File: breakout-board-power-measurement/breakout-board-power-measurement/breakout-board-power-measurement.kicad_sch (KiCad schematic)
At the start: 62 parts, among them J1 Screw_Terminal_01x04, J2 Conn_01x09, J3 Conn_01x07, J4 Conn_01x02, U1 MCP3911A0-E-SS, U2 Si8641BA-B-IU, U3 LM317_TO-252, Y1 10M

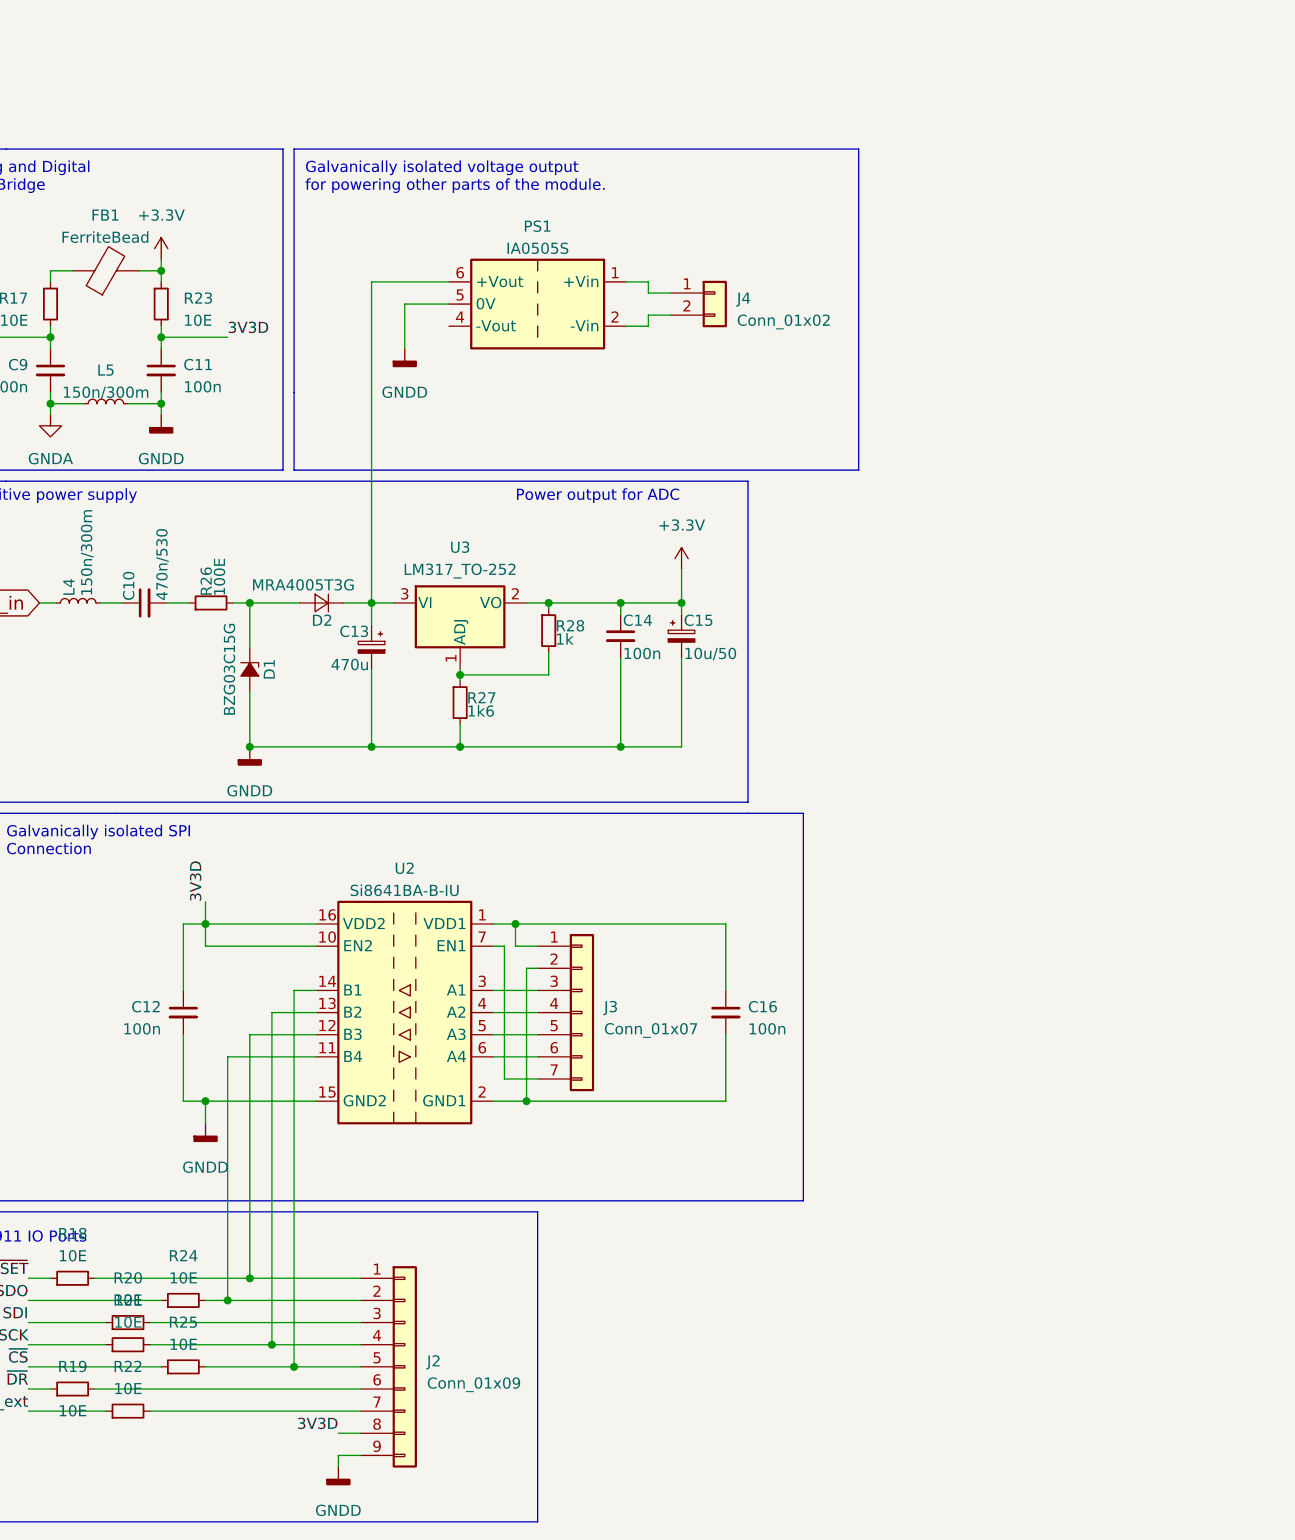
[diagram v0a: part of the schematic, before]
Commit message: Changed vias to test points
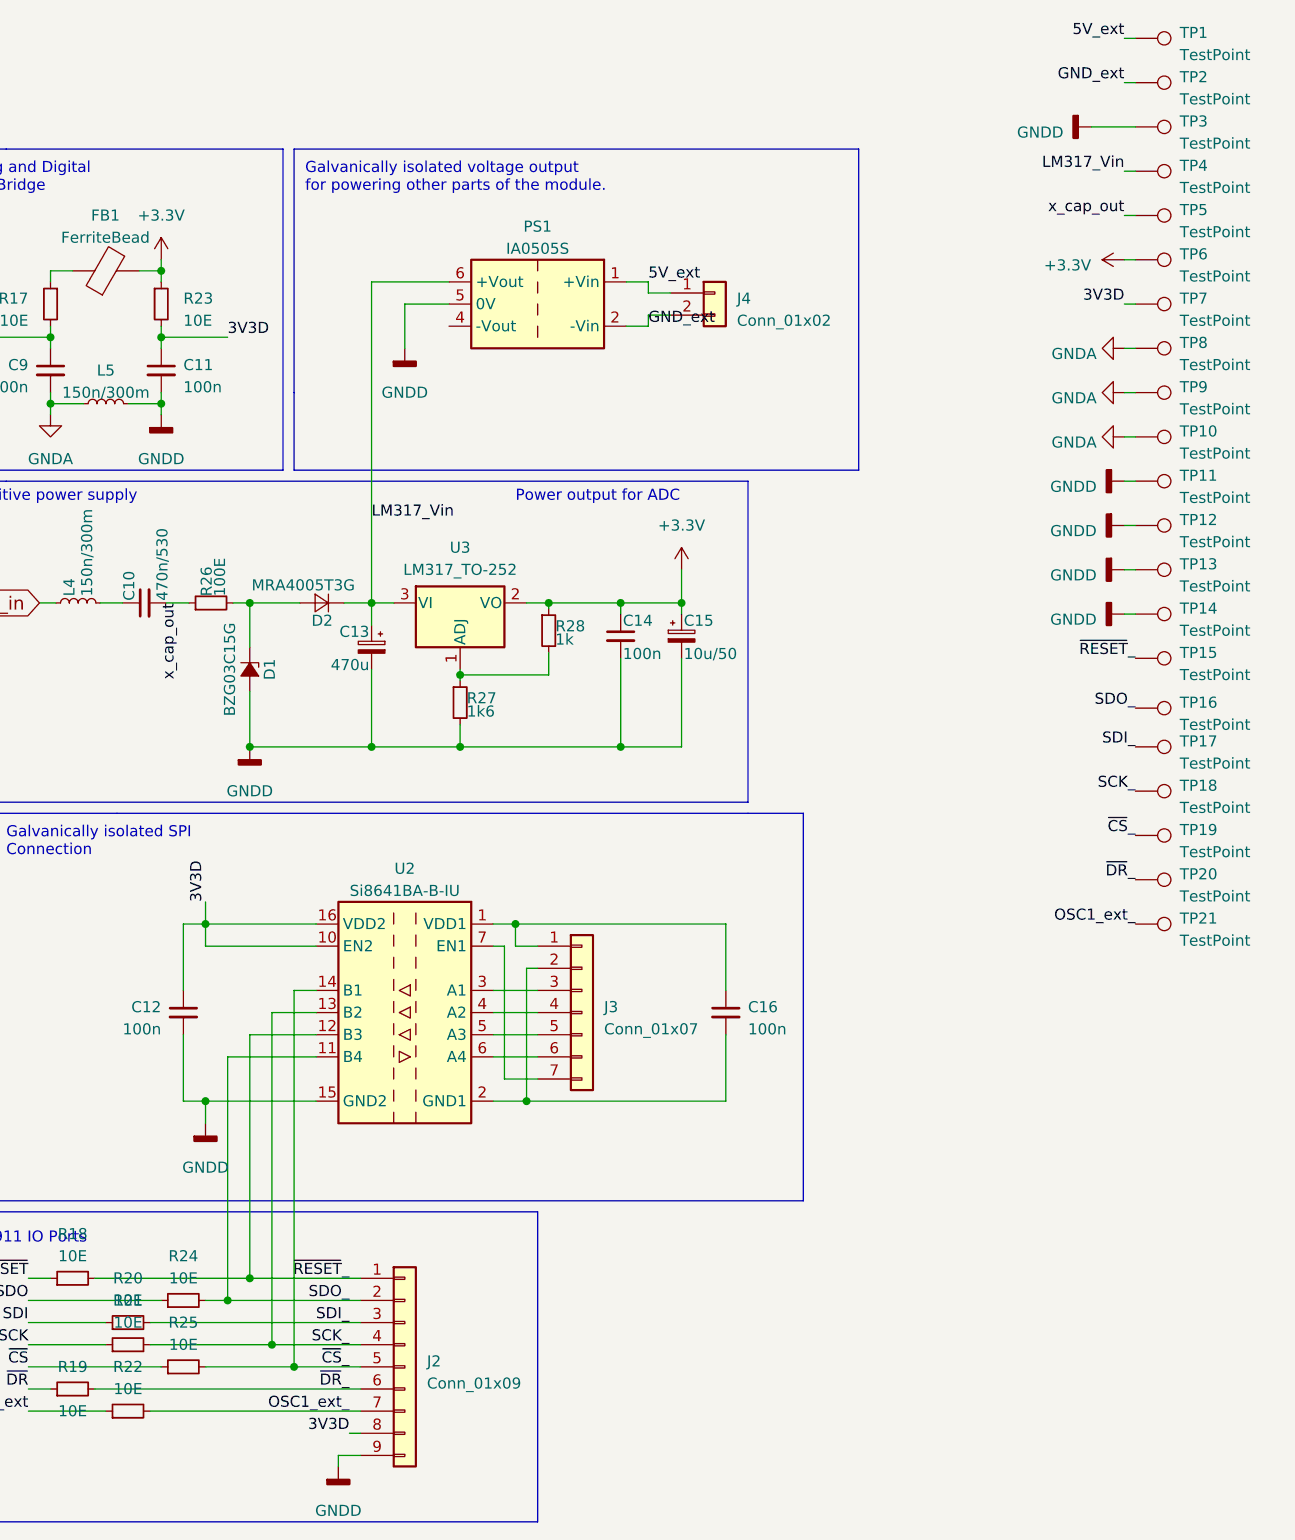
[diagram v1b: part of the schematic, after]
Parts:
- added TP1, TP10, TP11, TP12, TP13, TP14, TP15, TP16, TP17, TP18, TP19, TP2, TP20, TP21, TP3, TP4, TP5, TP6, TP7, TP8, TP9: TestPoint, TestPoint:TestPoint_THTPad_D1.0mm_Drill0.5mm, symbol Connector:TestPoint
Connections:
- net +3.3V: now also TP6.1
- net 3V3D: now also TP7.1
- net GNDA: now also TP10.1, TP8.1, TP9.1
- net GNDD: now also TP11.1, TP12.1, TP13.1, TP14.1, TP3.1
- net x_cap_out: now reaches C10.2, R26.1
- net x_cap_out: now also TP5.1
- net ~{RESET}_: now reaches J2.1 (Pin_1), R18.2, U2.12 (B3)
- net ~{RESET}_: now also TP15.1
- net SDO_: now reaches J2.2 (Pin_2), R24.2, U2.11 (B4)
- net SDO_: now also TP16.1
- net SDI_: now reaches J2.3 (Pin_3), R20.2
- net SDI_: now also TP17.1
- net SCK_: now reaches J2.4 (Pin_4), R21.2, U2.13 (B2)
- net SCK_: now also TP18.1
- net ~{CS}_: now reaches J2.5 (Pin_5), R25.2, U2.14 (B1)
- net ~{CS}_: now also TP19.1
- net ~{DR}_: now reaches J2.6 (Pin_6), R19.2
- net ~{DR}_: now also TP20.1
- net OSC1_ext_: now reaches J2.7 (Pin_7), R22.2
- net OSC1_ext_: now also TP21.1
- net 5V_ext: now reaches J4.1 (Pin_1), PS1.1 (+Vin)
- net 5V_ext: now also TP1.1
- net GND_ext: now reaches J4.2 (Pin_2), PS1.2 (-Vin)
- net GND_ext: now also TP2.1
- net LM317_Vin: now reaches C13.1, D2.1 (K), PS1.6 (+Vout), U3.3 (VI)
- net LM317_Vin: now also TP4.1

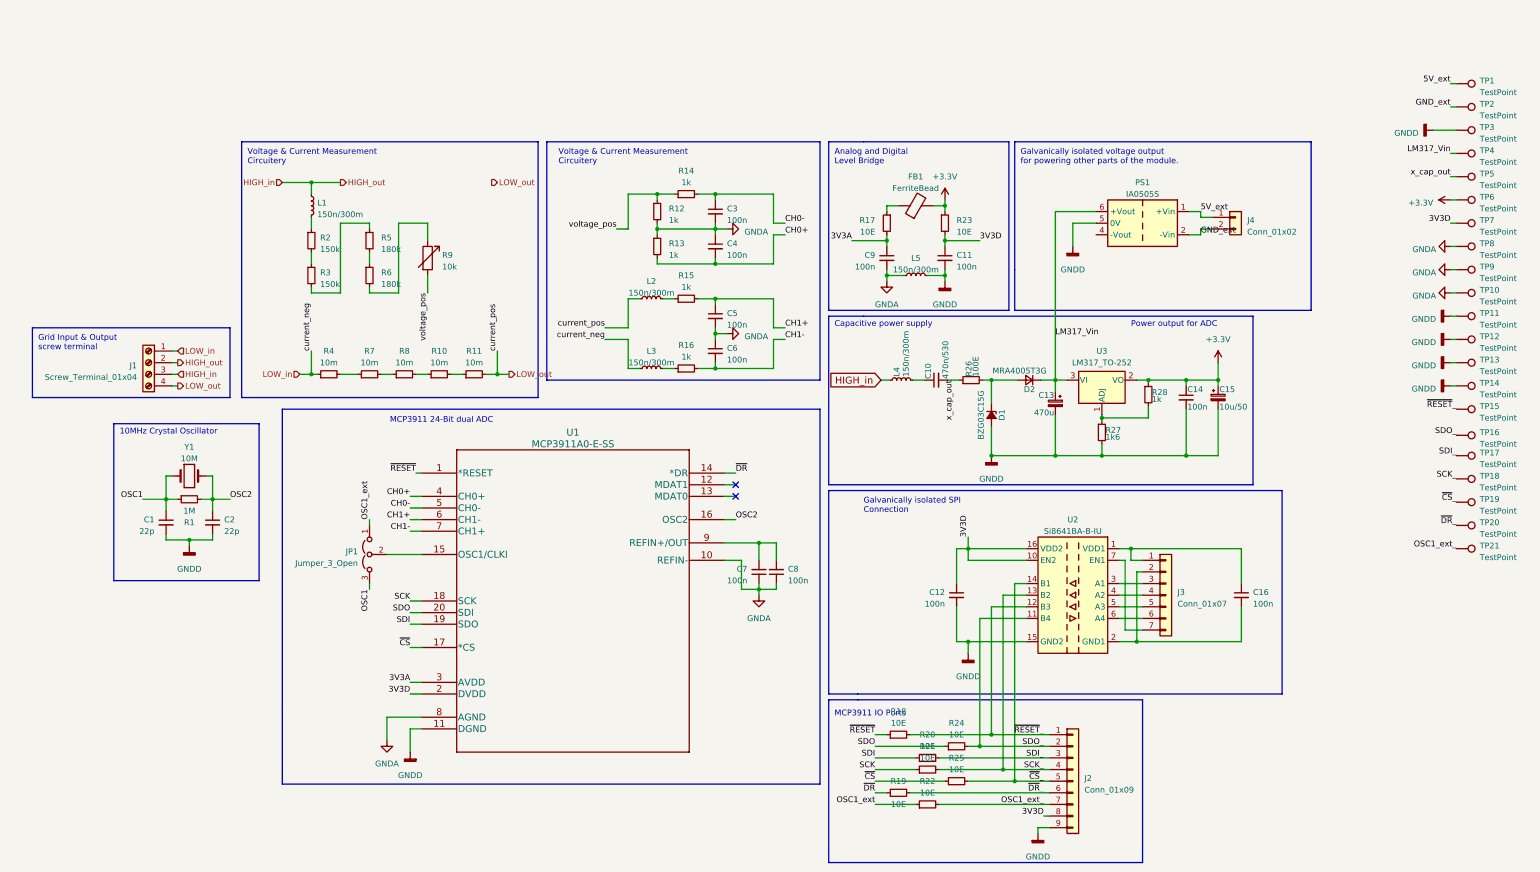
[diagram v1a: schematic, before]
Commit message: Fixed Power Measurement PCB, important changes.
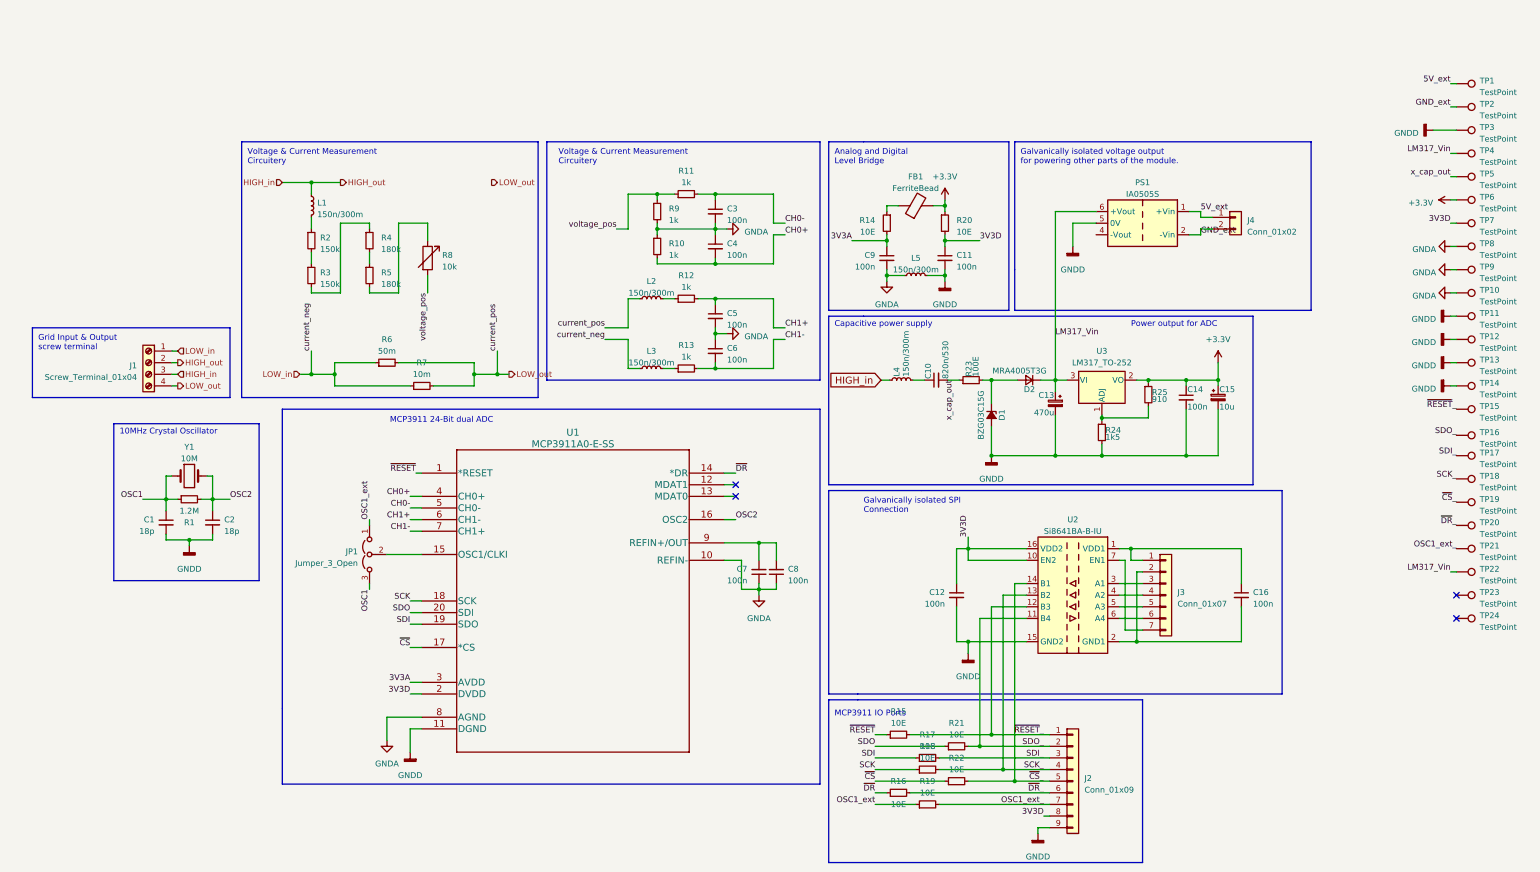
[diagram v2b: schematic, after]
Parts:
- removed R11, R4, R8: 10m, Resistor_SMD:R_1210_3225Metric, symbol Device:R_Small
- added TP22: TestPoint, Via:Via_THTPad_D1.5mm_Drill0.8mm, symbol Connector:TestPoint
- added TP23, TP24: TestPoint, Screwhole:Screwhole_THTPad_D3.0mm_Drill2.0mm, symbol Connector:TestPoint
- C1, C2: value 22p -> 18p
- C10: value 470n/530 -> 820n/530
- C13: footprint Capacitor_Tantalum_SMD:CP_EIA-7343-31_Kemet-D_Pad2.25x2.55mm_HandSolder -> Capacitor_THT:CP_Radial_D10.0mm_P5.00mm
- C15: value 10u/50 -> 10u; footprint Capacitor_Tantalum_SMD:CP_EIA-7343-31_Kemet-D_Pad2.25x2.55mm_HandSolder -> Capacitor_SMD:C_1206_3216Metric_Pad1.33x1.80mm_HandSolder
- D2: footprint Diode_SMD:D_SMA-SMB_Universal_Handsoldering -> Diode_SMD:D_MicroMELF_Handsoldering
- FB1: footprint Diode_SMD:D_SMA-SMB_Universal_Handsoldering -> Inductor_SMD:L_1210_3225Metric_Pad1.42x2.65mm_HandSolder
- R1: value 1M -> 1.2M
- R14: renamed from R17; footprint Resistor_SMD:R_1206_3216Metric_Pad1.30x1.75mm_HandSolder -> Resistor_SMD:R_0805_2012Metric_Pad1.20x1.40mm_HandSolder
- R15: renamed from R18; footprint Resistor_SMD:R_1206_3216Metric_Pad1.30x1.75mm_HandSolder -> Resistor_SMD:R_0805_2012Metric_Pad1.20x1.40mm_HandSolder
- R16: renamed from R19; footprint Resistor_SMD:R_1206_3216Metric_Pad1.30x1.75mm_HandSolder -> Resistor_SMD:R_0805_2012Metric_Pad1.20x1.40mm_HandSolder
- R17: renamed from R20; footprint Resistor_SMD:R_1206_3216Metric_Pad1.30x1.75mm_HandSolder -> Resistor_SMD:R_0805_2012Metric_Pad1.20x1.40mm_HandSolder
- R18: renamed from R21; footprint Resistor_SMD:R_1206_3216Metric_Pad1.30x1.75mm_HandSolder -> Resistor_SMD:R_0805_2012Metric_Pad1.20x1.40mm_HandSolder
- R19: renamed from R22; footprint Resistor_SMD:R_1206_3216Metric_Pad1.30x1.75mm_HandSolder -> Resistor_SMD:R_0805_2012Metric_Pad1.20x1.40mm_HandSolder
- R20: renamed from R23; footprint Resistor_SMD:R_1206_3216Metric_Pad1.30x1.75mm_HandSolder -> Resistor_SMD:R_0805_2012Metric_Pad1.20x1.40mm_HandSolder
- R21: renamed from R24; footprint Resistor_SMD:R_1206_3216Metric_Pad1.30x1.75mm_HandSolder -> Resistor_SMD:R_0805_2012Metric_Pad1.20x1.40mm_HandSolder
- R22: renamed from R25; footprint Resistor_SMD:R_1206_3216Metric_Pad1.30x1.75mm_HandSolder -> Resistor_SMD:R_0805_2012Metric_Pad1.20x1.40mm_HandSolder
- R24: renamed from R27; value 1k6 -> 1k5
- R25: renamed from R28; value 1k -> 910
- R6: renamed from R7; value 10m -> 50m; footprint Resistor_SMD:R_1210_3225Metric -> Resistor_SMD:R_2512_6332Metric
- R7: renamed from R10; footprint Resistor_SMD:R_1210_3225Metric -> Resistor_SMD:R_2512_6332Metric
- TP1, TP10, TP11, TP12, TP13, TP14, TP15, TP16, TP17, TP18, TP19, TP2, TP20, TP21, TP3, TP4, TP5, TP6, TP7, TP8, TP9: footprint TestPoint:TestPoint_THTPad_D1.0mm_Drill0.5mm -> Via:Via_THTPad_D1.5mm_Drill0.8mm
- renumbered R13 to R10, R14 to R11, R15 to R12, R16 to R13, R26 to R23, R5 to R4, R6 to R5, R9 to R8, R12 to R9
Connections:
- net LM317_Vin: now also TP22.1
- net LOW_in: now also R6.1, R7.1
- net LOW_out: now also R6.2, R7.2
- no-connect marks 2 -> 4
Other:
- moved on the sheet: R6, R7

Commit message: Minor fixes.
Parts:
- C1, C2: footprint Capacitor_SMD:C_1206_3216Metric_Pad1.33x1.80mm_HandSolder -> Capacitor_SMD:C_0805_2012Metric_Pad1.18x1.45mm_HandSolder
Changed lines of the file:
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@@
       (effects (font (size 1.27 1.27)) (justify left))
     )
-    (property "Footprint" "Capacitor_SMD:C_1206_3216Metric_Pad1.33x1.80mm_HandSolder" (at 57.15 135.255 0)
+    (property "Footprint" "Capacitor_SMD:C_0805_2012Metric_Pad1.18x1.45mm_HandSolder" (at 57.15 135.255 0)
       (effects (font (size 1.27 1.27)) hide)
     )
@@
       (effects (font (size 1.27 1.27)) (justify left))
     )
-    (property "Footprint" "Capacitor_SMD:C_1206_3216Metric_Pad1.33x1.80mm_HandSolder" (at 67.31 135.255 0)
-      (effects (font (size 1.27 1.27)) hide)
-    )
+    (property "Footprint" "Capacitor_SMD:C_0805_2012Metric_Pad1.18x1.45mm_HandSolder" (at 67.31 135.255 0)
+      (effects (font (size 1.27 1.27)) hide)
+    )
